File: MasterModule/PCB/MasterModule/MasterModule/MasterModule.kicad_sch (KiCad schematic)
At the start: 1 part

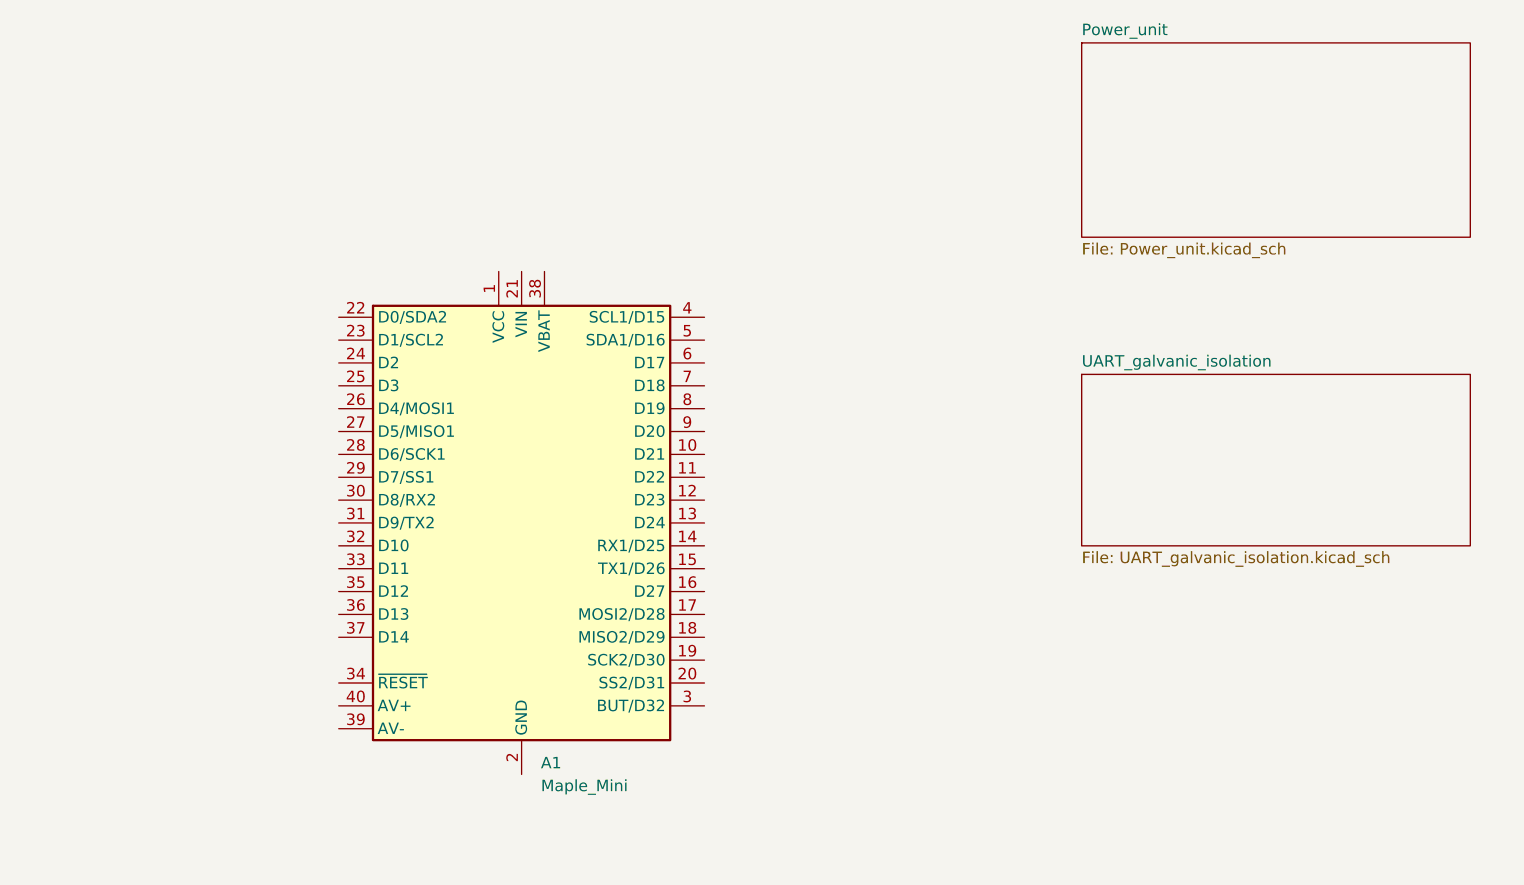
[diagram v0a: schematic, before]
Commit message: [PCB][MasterModule] Create MasterModule v.1.0
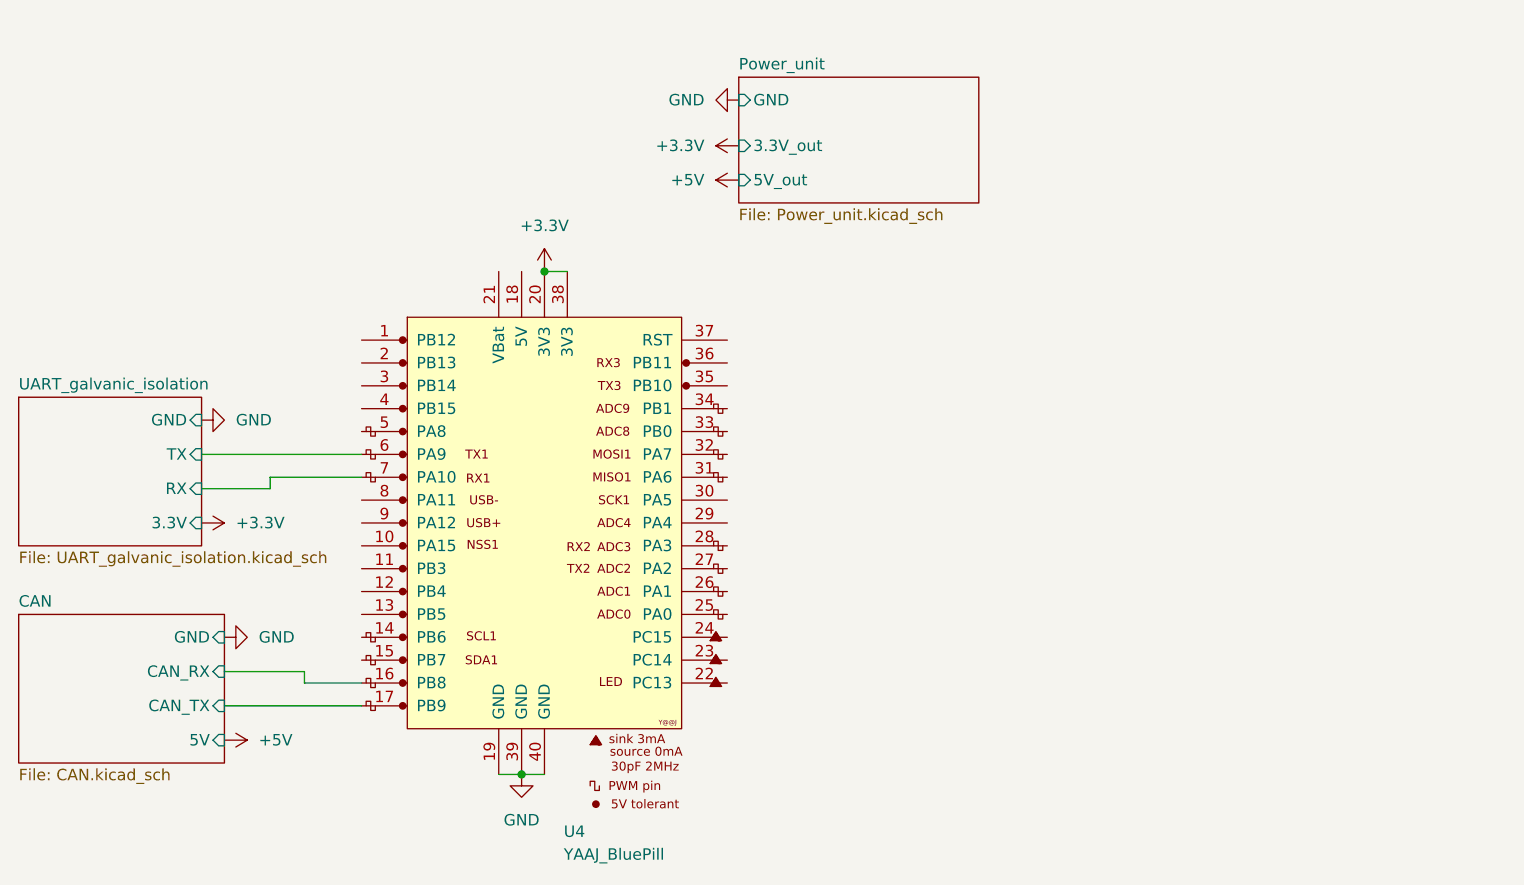
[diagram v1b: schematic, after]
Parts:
- removed A1: Maple_Mini, Module:Maple_Mini, symbol MCU_Module:Maple_Mini
- added U4: YAAJ_BluePill, STM32:YAAJ_BluePill_1, symbol STM32:YAAJ_BluePill
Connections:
- new net +3.3V: U4.20 (3V3), U4.38 (3V3)
- new net CAN/CAN_RX: U4.16 (PB8)
- new net CAN/CAN_TX: U4.17 (PB9)
- new net GND: U4.19 (GND), U4.39 (GND), U4.40 (GND)
- new net UART_galvanic_isolation/RX: U4.7 (PA10)
- new net UART_galvanic_isolation/TX: U4.6 (PA9)
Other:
- added sheet CAN (CAN.kicad_sch)
- sheet Power_unit ports: added 3.3V_out, 5V_out, GND; removed none
- sheet UART_galvanic_isolation ports: added 3.3V, GND, RX, TX; removed none
